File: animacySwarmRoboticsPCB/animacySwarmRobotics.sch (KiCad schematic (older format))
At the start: 90 parts, among them J1 Conn_01x04, J10 Conn_01x03, J11 Conn_01x03, J12 Conn_01x01, J13 Conn_01x03, J14 Conn_01x03, J15 Conn_01x01, J16 Conn_01x01, J17 Conn_01x01, J18 Conn_01x01, J19 Conn_01x03, J2 Conn_01x04, J20 Conn_01x03, J21 Conn_01x01, J22 Conn_01x01, J23 Conn_01x01, J24 Conn_01x01, J25 Conn_01x03, J26 Conn_01x03, J27 Conn_01x03, J28 Conn_01x03, J29 Conn_01x03, J3 Conn_01x03, J30 Conn_01x03, J4 Conn_01x03, SW2 SW_Push, SW3 SW_Push, U1 Seeduino, U10 NJM2746M, U4 NJM2746M, U5 NJM2746M, U6 NJM2746M, U8 NJM2746M, U9 NJM2746M

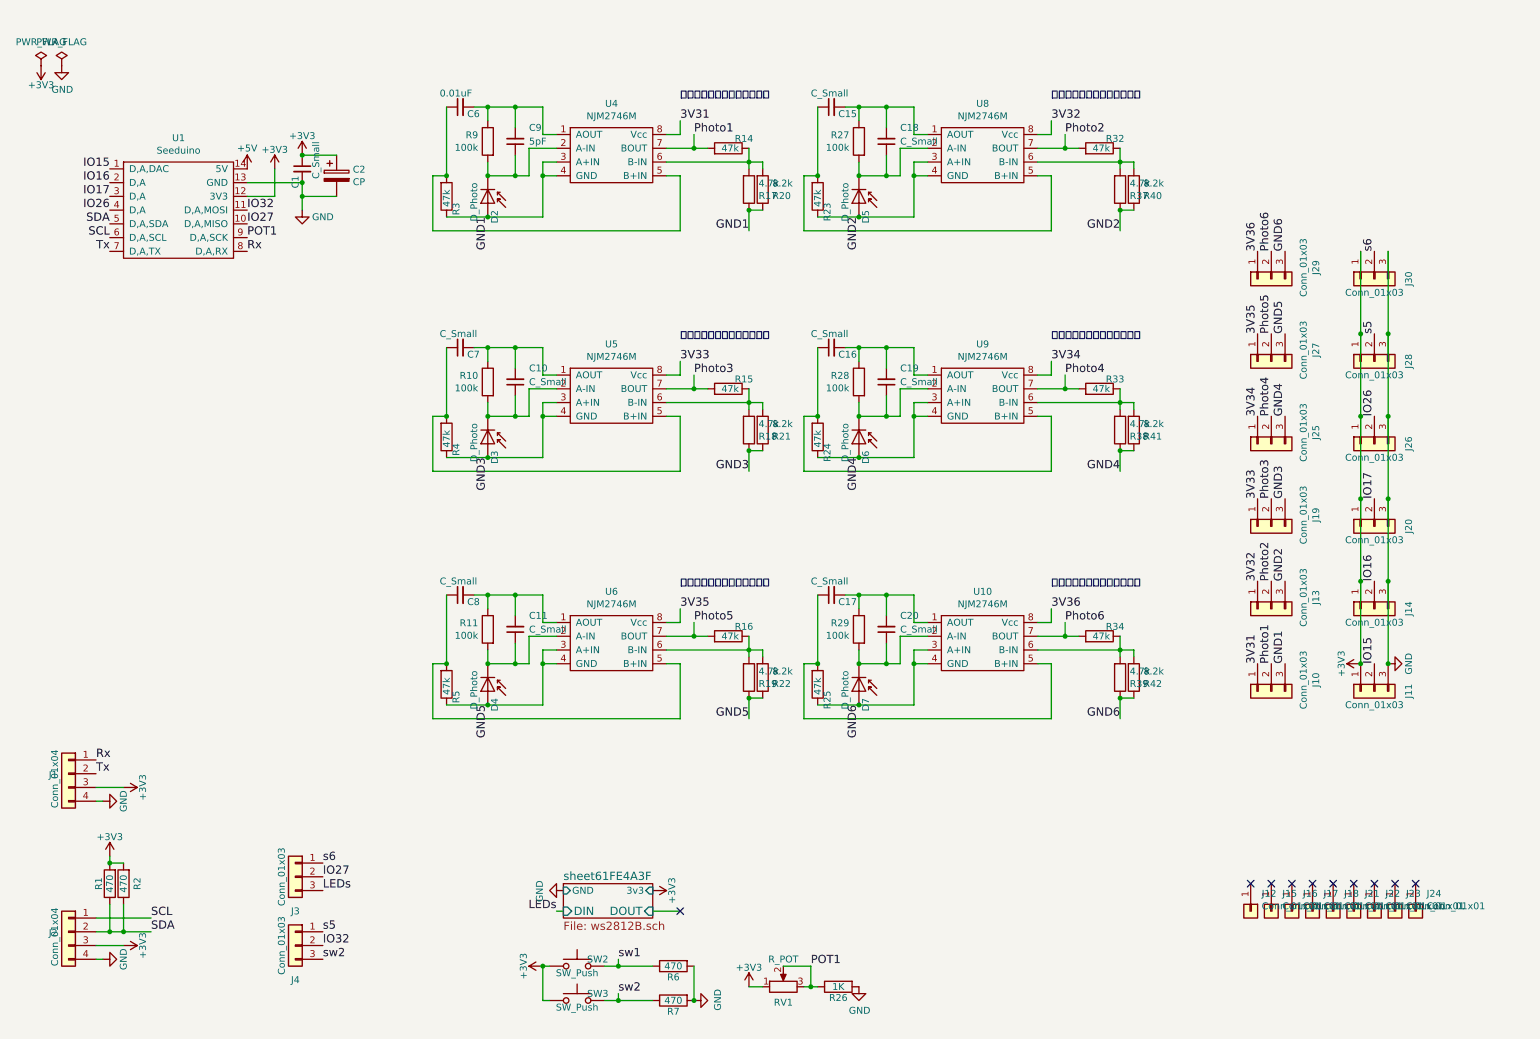
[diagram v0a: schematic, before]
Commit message: fix schematic because i changed failue project...
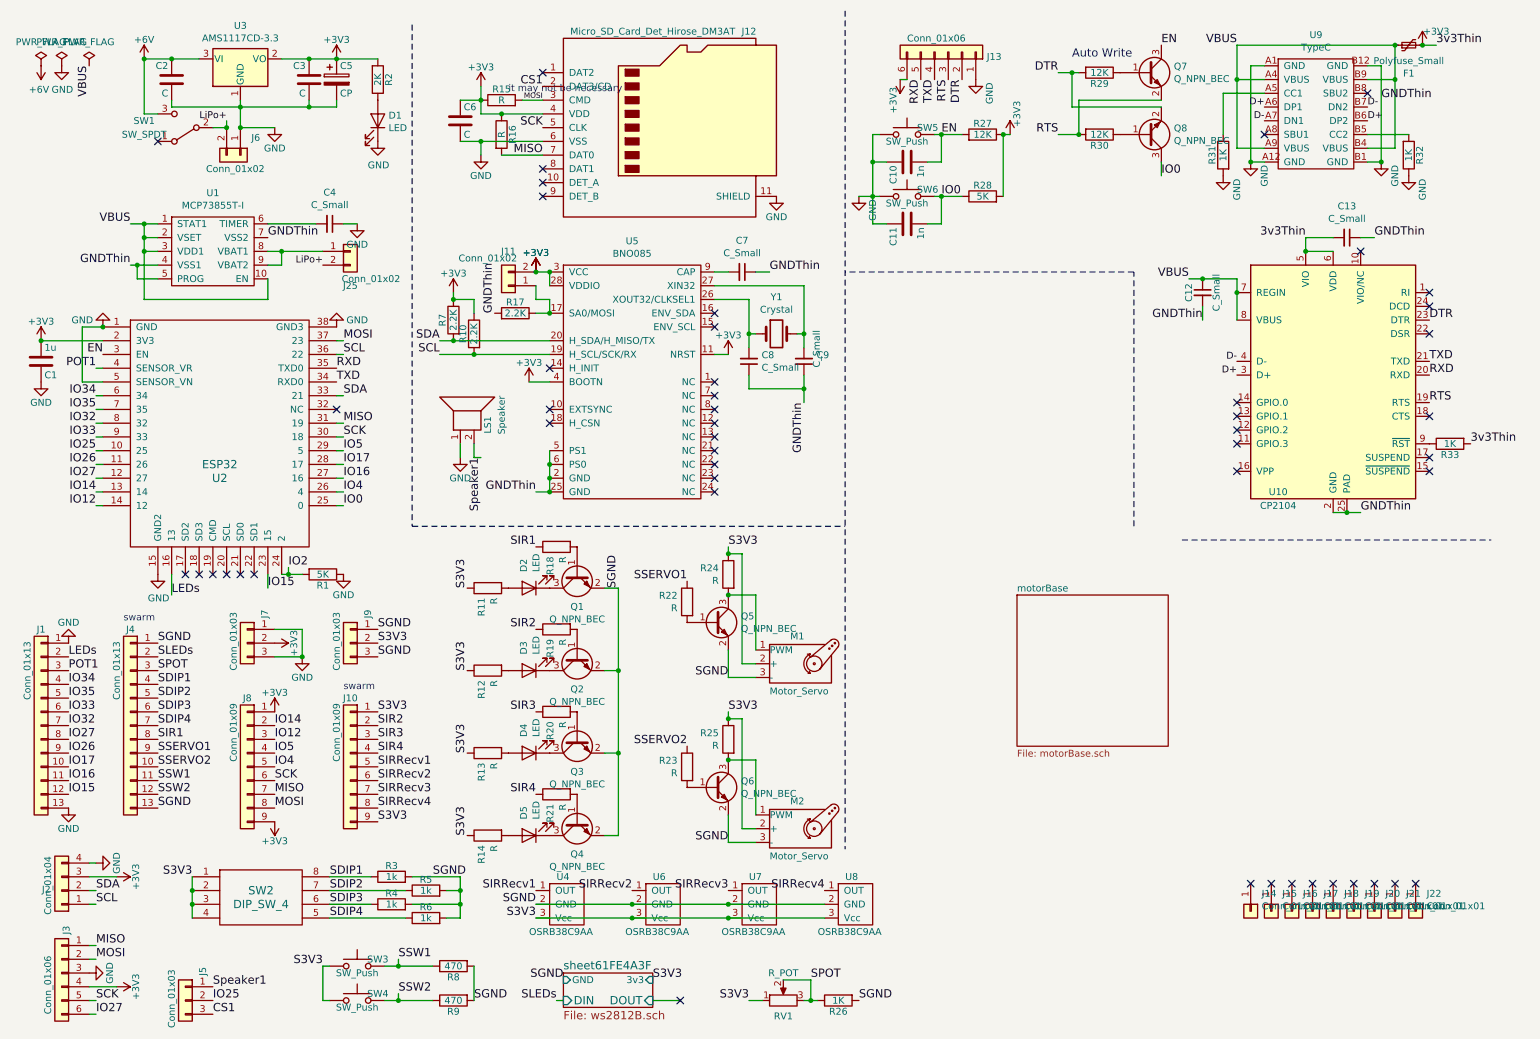
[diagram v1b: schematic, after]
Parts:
- removed C1, C15, C16, C17: C_Small, Capacitor_THT:C_Disc_D3.0mm_W1.6mm_P2.50mm, symbol Device:C_Small
- removed C10, C11, C18, C19, C20: C_Small, Capacitor_THT:C_Disc_D5.0mm_W2.5mm_P5.00mm, symbol Device:C_Small
- removed C2: CP, Capacitor_SMD:CP_Elec_6.3x7.7, symbol Device:CP
- removed C6: 0.01uF, Capacitor_THT:C_Disc_D3.0mm_W1.6mm_P2.50mm, symbol Device:C_Small
- removed D2, D3, D4, D5, D6, D7: D_Photo, symbol Device:D_Photo
- removed J1: Conn_01x04, Connector:NS-Tech_Grove_1x04_P2mm_Vertical, symbol Connector_Generic:Conn_01x04
- removed J10, J11, J13, J14, J19, J20, J25, J26, J27, J28, J29, J30: Conn_01x03, Connector_JST:JST_XH_B3B-XH-A_1x03_P2.50mm_Vertical, symbol Connector_Generic:Conn_01x03
- removed J3, J4: Conn_01x03, Jumper:SolderJumper-3_P1.3mm_Open_Pad1.0x1.5mm, symbol Connector_Generic:Conn_01x03
- removed R14, R34: 47k, Resistor_THT:R_Axial_DIN0204_L3.6mm_D1.6mm_P5.08mm_Horizontal, symbol Device:R
- removed R37, R38, R39: 4.7k, Resistor_THT:R_Axial_DIN0204_L3.6mm_D1.6mm_P5.08mm_Horizontal, symbol Device:R
- removed R40, R41, R42: 8.2k, Resistor_THT:R_Axial_DIN0204_L3.6mm_D1.6mm_P5.08mm_Horizontal, symbol Device:R
- removed U1: Seeduino, symbol ume-boshi:Seeduino
- removed U10, U4, U5, U6, U8, U9: NJM2746M, symbol ume-boshi:NJM2746M
- added C1: 1u, akizukit:SMD-2012, symbol Device:C
- added C10, C11: 1n, akizukit:SMD-2012, symbol Device:C
- added C12, C13, C4: C_Small, akizukit:SMD-2012, symbol Device:C_Small
- added C2, C3, C6: C, akizukit:SMD-2012, symbol Device:C
- added C5: CP, Capacitor_SMD:C_Elec_6.3x7.7, symbol Device:CP
- added D1: LED, akizukit:2012LED, symbol Device:LED
- added D2, D3, D4, D5: LED, LED_THT:LED_D3.0mm, symbol Device:LED
- added F1: Polyfuse_Small, akizukit:SMD-1608, symbol Device:Polyfuse_Small
- added J1, J4: Conn_01x13, Connector_PinHeader_2.54mm:PinHeader_1x13_P2.54mm_Vertical, symbol Connector_Generic:Conn_01x13
- added J10, J8: Conn_01x09, Connector_PinHeader_2.54mm:PinHeader_1x09_P2.54mm_Vertical, symbol Connector_Generic:Conn_01x09
- added J11, J25: Conn_01x02, Jumper:SolderJumper-2_P1.3mm_Open_Pad1.0x1.5mm, symbol Connector_Generic:Conn_01x02
- added J12: Micro_SD_Card_Det_Hirose_DM3AT, akizukit:SD_DM3AT-SF-PEJMS, symbol Connector:Micro_SD_Card_Det_Hirose_DM3AT
- added J13: Conn_01x06, Connector_PinHeader_2.54mm:PinHeader_1x06_P2.54mm_Horizontal, symbol Connector_Generic:Conn_01x06
- added J3: Conn_01x06, Connector_PinHeader_1.27mm:PinHeader_1x06_P1.27mm_Vertical, symbol Connector_Generic:Conn_01x06
- added J5: Conn_01x03, Jumper:SolderJumper-3_P1.3mm_Open_Pad1.0x1.5mm, symbol Connector_Generic:Conn_01x03
- added J6: Conn_01x02, akizukit:Connector_EH_2pin, symbol Connector_Generic:Conn_01x02
- added J7, J9: Conn_01x03, Connector_PinHeader_2.54mm:PinHeader_1x03_P2.54mm_Vertical, symbol Connector_Generic:Conn_01x03
- added LS1: Speaker, akizukit:small_speaker, symbol Device:Speaker
- added M1, M2: Motor_Servo, Connector_PinHeader_2.54mm:PinHeader_1x03_P2.54mm_Vertical, symbol Motor:Motor_Servo
- added Q1, Q2, Q3, Q4, Q5, Q6, Q7, Q8: Q_NPN_BEC, Package_TO_SOT_SMD:SC-59_Handsoldering, symbol Device:Q_NPN_BEC
- added R12, R13: R, akizukit:SMD-1608, symbol Device:R
- added R30: 12K, akizukit:SMD-1608, symbol Device:R
- added R31: 1K, akizukit:SMD-1608, symbol Device:R
- added R6: 1k, akizukit:SMD-1608, symbol Device:R
- added R7: 2.2K, akizukit:SMD-1608, symbol Device:R
- added SW1: SW_SPDT, Connector_PinHeader_2.54mm:PinHeader_1x03_P2.54mm_Vertical, symbol Switch:SW_SPDT
- added SW2: DIP_SW_4, akizukit:EHS104LD, symbol ume-boshi:DIP_SW_4
- added SW5, SW6: SW_Push, Button_Switch_THT:SW_Tactile_SPST_Angled_PTS645Vx39-2LFS, symbol Switch:SW_Push
- added U1: MCP73855T-I, akizukit:MCP73855, symbol ume-boshi:MCP73855T-I
- added U10: CP2104, Package_DFN_QFN:QFN-24-1EP_4x4mm_P0.5mm_EP2.6x2.6mm, symbol Interface_USB:CP2104
- added U2: ESP32, akizukit:ESP-WROOM-32, symbol akizukit:ESP32
- added U3: AMS1117CD-3.3, akizukit:AZ1086H, symbol Regulator_Linear:AMS1117CD-3.3
- added U4, U6, U7, U8: OSRB38C9AA, Connector_PinHeader_1.27mm:PinHeader_1x03_P1.27mm_Vertical, symbol ume-boshi:OSRB38C9AA
- added U5: BNO085, Package_LGA:LGA-28_5.2x3.8mm_P0.5mm, symbol ume-boshi:BNO085
- added U9: TypeC, Connector_USB:USB_C_Receptacle_HRO_TYPE-C-31-M-12, symbol akizukit:TypeC
- added Y1: Crystal, akizukit:FC-135, symbol Device:Crystal
- C7, C8: footprint Capacitor_THT:C_Disc_D3.0mm_W1.6mm_P2.50mm -> akizukit:SMD-2012
- C9: value 5pF -> C_Small; footprint Capacitor_THT:C_Disc_D5.0mm_W2.5mm_P5.00mm -> akizukit:SMD-2012
- R1: value 470 -> 5K
- R10: value 100k -> 2.2K; footprint Resistor_THT:R_Axial_DIN0204_L3.6mm_D1.6mm_P5.08mm_Horizontal -> akizukit:SMD-1608
- R11: value 100k -> R; footprint Resistor_THT:R_Axial_DIN0204_L3.6mm_D1.6mm_P5.08mm_Horizontal -> akizukit:SMD-1608
- R14: renamed from R9; value 100k -> R; footprint Resistor_THT:R_Axial_DIN0204_L3.6mm_D1.6mm_P5.08mm_Horizontal -> akizukit:SMD-1608
- R15, R16, R23, R24, R25: value 47k -> R; footprint Resistor_THT:R_Axial_DIN0204_L3.6mm_D1.6mm_P5.08mm_Horizontal -> akizukit:SMD-1608
- R17: value 4.7k -> 2.2K; footprint Resistor_THT:R_Axial_DIN0204_L3.6mm_D1.6mm_P5.08mm_Horizontal -> akizukit:SMD-1608
- R18, R19: value 4.7k -> R; footprint Resistor_THT:R_Axial_DIN0204_L3.6mm_D1.6mm_P5.08mm_Horizontal -> akizukit:SMD-1608
- R2: value 470 -> 2K
- R20, R21, R22: value 8.2k -> R; footprint Resistor_THT:R_Axial_DIN0204_L3.6mm_D1.6mm_P5.08mm_Horizontal -> akizukit:SMD-1608
- R27, R29: value 100k -> 12K; footprint Resistor_THT:R_Axial_DIN0204_L3.6mm_D1.6mm_P5.08mm_Horizontal -> akizukit:SMD-1608
- R28: value 100k -> 5K; footprint Resistor_THT:R_Axial_DIN0204_L3.6mm_D1.6mm_P5.08mm_Horizontal -> akizukit:SMD-1608
- R3, R4, R5: value 47k -> 1k; footprint Resistor_THT:R_Axial_DIN0204_L3.6mm_D1.6mm_P5.08mm_Horizontal -> akizukit:SMD-1608
- R32, R33: value 47k -> 1K; footprint Resistor_THT:R_Axial_DIN0204_L3.6mm_D1.6mm_P5.08mm_Horizontal -> akizukit:SMD-1608
- SW3: renamed from SW2; footprint Button_Switch_THT:SW_PUSH_6mm_H7.3mm -> akizukit:SMD_SW
- SW4: renamed from SW3; footprint Button_Switch_THT:SW_PUSH_6mm_H7.3mm -> akizukit:SMD_SW
- renumbered J12 to J14, J21 to J19, J22 to J20, J23 to J21, J24 to J22, R6 to R8, R7 to R9
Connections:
- net GND6 is gone; now on net S3V3: R25.1
- net Photo4 is gone; now on net +3V3: R33.2
- net +3V3: now also R10.1, R15.1, R16.1, R27.1, R28.2, C1.2, C13.2, C3.1, C5.1, C6.1, F1.2, J11.2 (Pin_2), J12.4 (VDD), J13.6 (Pin_6), J3.4 (Pin_4), J7.2 (Pin_2), J8.1 (Pin_1), J8.9 (Pin_9), R7.1, U10.5 (VIO), U10.6 (VDD), U2.2 (3V3), U3.2 (VO), U5.11 (NRST), U5.28 (VDDIO), U5.3 (VCC), U5.4 (BOOTN); no longer R1.2, RV1.1, SW3.1, SW4.1
- net GND: now also C7.1, C8.1, C9.1, R1.1, R17.2, R32.1, C1.1, C10.1, C11.1, C12.2, C13.1, C2.2, C3.2, C4.1, C5.2, C6.2, D1.1 (K), J1.1 (Pin_1), J1.13 (Pin_13), J12.11 (SHIELD), J12.6 (VSS), J13.1 (Pin_1), J3.3 (Pin_3), J6.1 (Pin_1), J7.1 (Pin_1), J7.3 (Pin_3), LS1.1, R31.2, SW5.1, SW6.1, U1.4 (VSS1), U1.5 (PROG), U1.7 (VSS2), U10.2 (GND), U10.25 (PAD), U2.1 (GND), U2.15 (GND2), U2.38 (GND3), U2.5 (SENSOR_VN), U3.1 (GND), U5.2 (GND), U5.25 (GND), U5.5 (PS1), U5.6 (PS0), U9.A1 (GND), U9.A12 (GND), U9.B1 (GND), U9.B12 (GND); no longer R26.2, R8.2, R9.2
- net IO15: now also J1.12 (Pin_12), U2.23 (15)
- net IO16: now also J1.11 (Pin_11), U2.27 (16)
- net IO17: now also J1.10 (Pin_10), U2.28 (17)
- net IO26: now also J1.9 (Pin_9), U2.11 (26)
- net IO27: now also J1.8 (Pin_8), J3.6 (Pin_6), U2.12 (27)
- net IO32: now also J1.7 (Pin_7), U2.8 (32)
- net LEDs: now also J1.2 (Pin_2), U2.16 (13)
- net POT1: now also J1.3 (Pin_3), U2.4 (SENSOR_VR); no longer R26.1, RV1.2, RV1.3
- net SCL: now also R10.2, U2.36 (22), U5.19 (H_SCL/SCK/RX)
- net SDA: now also R7.2, U2.33 (21), U5.20 (H_SDA/H_MISO/TX); no longer R1.1, R2.1
- net at R14.2: now also D5.2 (A); no longer C9.1
- net at C9.2: now also U5.27 (XIN32), Y1.2; no longer R14.1
- net SGND: now reaches R3.2
- net SGND: now also R26.2, R4.2, R5.2, R8.2, R9.2, J4.1 (Pin_1), J4.13 (Pin_13), J9.1 (Pin_1), J9.3 (Pin_3), M1.3 (-), M2.3 (-), Q1.2 (E), Q2.2 (E), Q3.2 (E), Q4.2 (E), Q5.2 (E), Q6.2 (E), R6.2, U4.2 (GND), U6.2 (GND), U7.2 (GND), U8.2 (GND)
- net at R20.2: now also Q3.1 (B); no longer R17.2
- net EN: now reaches R27.2
- net EN: now also C10.2, Q7.3 (C), SW5.2, U2.3 (EN)
- net at R23.2: now also Q6.1 (B)
- net at C7.2: now also U5.9 (CAP); no longer R10.1
- net IO0: now reaches R28.1
- net IO0: now also C11.2, Q8.3 (C), SW6.2, U2.25 (0)
- net at R24.2: now also M1.1 (PWM), Q5.3 (C)
- net at R33.1: now also U10.9 (~RST)
- net at C8.2: now also U5.26 (XOUT32/CLKSEL1), Y1.1; no longer R11.1
- net at R11.2: now also D2.2 (A)
- net at R29.1: now also Q7.1 (B)
- net DTR: now reaches R29.2
- net DTR: now also J13.2 (Pin_2), Q8.2 (E), U10.23 (DTR)
- net at R25.2: now also M2.1 (PWM), Q6.3 (C)
- removed net GND1: R17.1, R20.1, R3.1
- net GND2 renamed SSERVO2
- net SSERVO2: now also J4.10 (Pin_10)
- removed net GND3: R18.1, R21.1, R4.1
- net GND4 renamed S3V3
- net S3V3: now also R11.1, R14.1, RV1.1, SW3.1, SW4.1, J10.1 (Pin_1), J10.9 (Pin_9), J9.2 (Pin_2), M1.2 (+), M2.2 (+), R12.1, R13.1, SW2.1, SW2.2, SW2.3, SW2.4, U4.3 (Vcc), U6.3 (Vcc), U7.3 (Vcc), U8.3 (Vcc)
- removed net GND5: R19.1, R22.1, R5.1
- net Photo2: no longer names the net of R32.2
- net Photo2: now also U9.B5 (CC2)
- net Photo3 renamed MOSI
- net MOSI: now also J12.3 (CMD), J3.2 (Pin_2), J8.8 (Pin_8), U2.37 (23)
- net Photo5 renamed MISO
- net MISO: now also J12.7 (DAT0), J3.1 (Pin_1), J8.7 (Pin_7), U2.31 (19)
- net sw1 renamed SSW1
- net SSW1: now also J4.11 (Pin_11)
- net sw2 renamed SSW2
- net SSW2: now also J4.12 (Pin_12)
- new net: Q8.1 (B), R30.1
- new net: R31.1, U9.A5 (CC1)
- new net: D4.1 (K), Q3.3 (C)
- new net: D4.2 (A), R13.2
- new net: D5.1 (K), Q4.3 (C)
- new net: Q4.1 (B), R21.2
- new net: D3.1 (K), Q2.3 (C)
- new net: D3.2 (A), R12.2
- new net: Q2.1 (B), R19.2
- new net: D2.1 (K), Q1.3 (C)
- new net: Q1.1 (B), R18.2
- new net: J11.1 (Pin_1), R17.1, U5.17 (SA0/MOSI)
- new net: C4.2, U1.6 (TIMER)
- new net: J25.1 (Pin_1), U1.8 (VBAT1), U1.9 (VBAT2)
- new net: D1.2 (A), R2.1
- new net: Q5.1 (B), R22.2
- new net +6V: C2.1, SW1.3 (C), U3.3 (VI)
- new net CS1: J12.2 (DAT3/CD), J5.3 (Pin_3)
- new net D+: U10.3 (D+), U9.A6 (DP1), U9.B6 (DP2)
- new net D-: U10.4 (D-), U9.A7 (DN1), U9.B7 (DN2)
- new net IO12: J8.3 (Pin_3), U2.14 (12)
- new net IO14: J8.2 (Pin_2), U2.13 (14)
- new net IO2: R1.2, U2.24 (2)
- new net IO25: J5.2 (Pin_2), U2.10 (25)
- new net IO33: J1.6 (Pin_6), U2.9 (33)
- new net IO34: J1.4 (Pin_4), U2.6 (34)
- new net IO35: J1.5 (Pin_5), U2.7 (35)
- new net IO4: J8.5 (Pin_5), U2.26 (4)
- new net IO5: J8.4 (Pin_4), U2.29 (5)
- new net LiPo+: J25.2 (Pin_2), J6.2 (Pin_2), SW1.2 (B)
- new net RTS: J13.3 (Pin_3), Q7.2 (E), R30.2, U10.19 (RTS)
- new net RXD: J13.5 (Pin_5), U10.20 (RXD), U2.35 (TXD0)
- new net SCK: J12.5 (CLK), J3.5 (Pin_5), J8.6 (Pin_6), U2.30 (18)
- new net SDIP1: J4.4 (Pin_4), R3.1, SW2.8
- new net SDIP2: J4.5 (Pin_5), R5.1, SW2.7
- new net SDIP3: J4.6 (Pin_6), R4.1, SW2.6
- new net SDIP4: J4.7 (Pin_7), R6.1, SW2.5
- new net SIR1: J4.8 (Pin_8), R18.1
- new net SIR2: J10.2 (Pin_2), R19.1
- new net SIR3: J10.3 (Pin_3), R20.1
- new net SIR4: J10.4 (Pin_4), R21.1
- new net SIRRecv1: J10.5 (Pin_5), U4.1 (OUT)
- new net SIRRecv2: J10.6 (Pin_6), U6.1 (OUT)
- new net SIRRecv3: J10.7 (Pin_7), U7.1 (OUT)
- new net SIRRecv4: J10.8 (Pin_8), U8.1 (OUT)
- new net SLEDs: J4.2 (Pin_2)
- new net SPOT: J4.3 (Pin_3), R26.1, RV1.2, RV1.3
- new net SSERVO1: J4.9 (Pin_9), R22.1
- new net Speaker1: J5.1 (Pin_1), LS1.2
- new net TXD: J13.4 (Pin_4), U10.21 (TXD), U2.34 (RXD0)
- new net VBUS: C12.1, F1.1, U1.1 (STAT1), U1.10 (EN), U1.2 (VSET), U1.3 (VDD1), U10.7 (REGIN), U10.8 (VBUS), U9.A4 (VBUS), U9.A9 (VBUS), U9.B4 (VBUS), U9.B9 (VBUS)
- no-connect marks 10 -> 50
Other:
- note added: "Auto Write"
- note added: "it may not be necessary"
- note added: "swarm"
- note removed: "スルーホールの部品を用いる"
- moved on the sheet: J2, R14, R26, R8, R9, RV1, SW3, SW4
